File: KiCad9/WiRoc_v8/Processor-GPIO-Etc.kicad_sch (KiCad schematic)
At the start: 6 parts

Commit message: etc
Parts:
- R33, R35: LCSC Part # (none) -> C25804; Manufacturer (none) -> Uniroyal Elec; ManufacturerPartNumber (none) -> 0603WAF1002T5E
- U11: value ~ -> AllwinnerH3
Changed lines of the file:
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@@
 			)
 		)
-		(property "Value" "~"
+		(property "Value" "AllwinnerH3"
 			(at 96.52 68.58 0)
 			(effects
@@
 			)
 		)
-		(property "Value" "~"
+		(property "Value" "AllwinnerH3"
 			(at 232.41 127 0)
 			(effects
@@
 		(property "Description" ""
 			(at 254 121.92 0)
+			(effects
+				(font
+					(size 1.27 1.27)
+				)
+				(hide yes)
+			)
+		)
+		(property "LCSC Part #" "C25804"
+			(at 254 121.92 90)
+			(effects
+				(font
+					(size 1.27 1.27)
+				)
+				(hide yes)
+			)
+		)
+		(property "Manufacturer" "Uniroyal Elec"
+			(at 254 121.92 90)
+			(effects
+				(font
+					(size 1.27 1.27)
+				)
+				(hide yes)
+			)
+		)
+		(property "ManufacturerPartNumber" "0603WAF1002T5E"
+			(at 254 121.92 90)
 			(effects
 				(font
@@
 			)
 		)
+		(property "LCSC Part #" "C25804"
+			(at 251.46 114.3 90)
+			(effects
+				(font
+					(size 1.27 1.27)
+				)
+				(hide yes)
+			)
+		)
+		(property "Manufacturer" "Uniroyal Elec"
+			(at 251.46 114.3 90)
+			(effects
+				(font
+					(size 1.27 1.27)
+				)
+				(hide yes)
+			)
+		)
+		(property "ManufacturerPartNumber" "0603WAF1002T5E"
+			(at 251.46 114.3 90)
+			(effects
+				(font
+					(size 1.27 1.27)
+				)
+				(hide yes)
+			)
+		)
 		(pin "2"
 		)
@@
 			)
 		)
-		(property "Value" "~"
+		(property "Value" "AllwinnerH3"
 			(at 231.14 67.31 0)
 			(effects

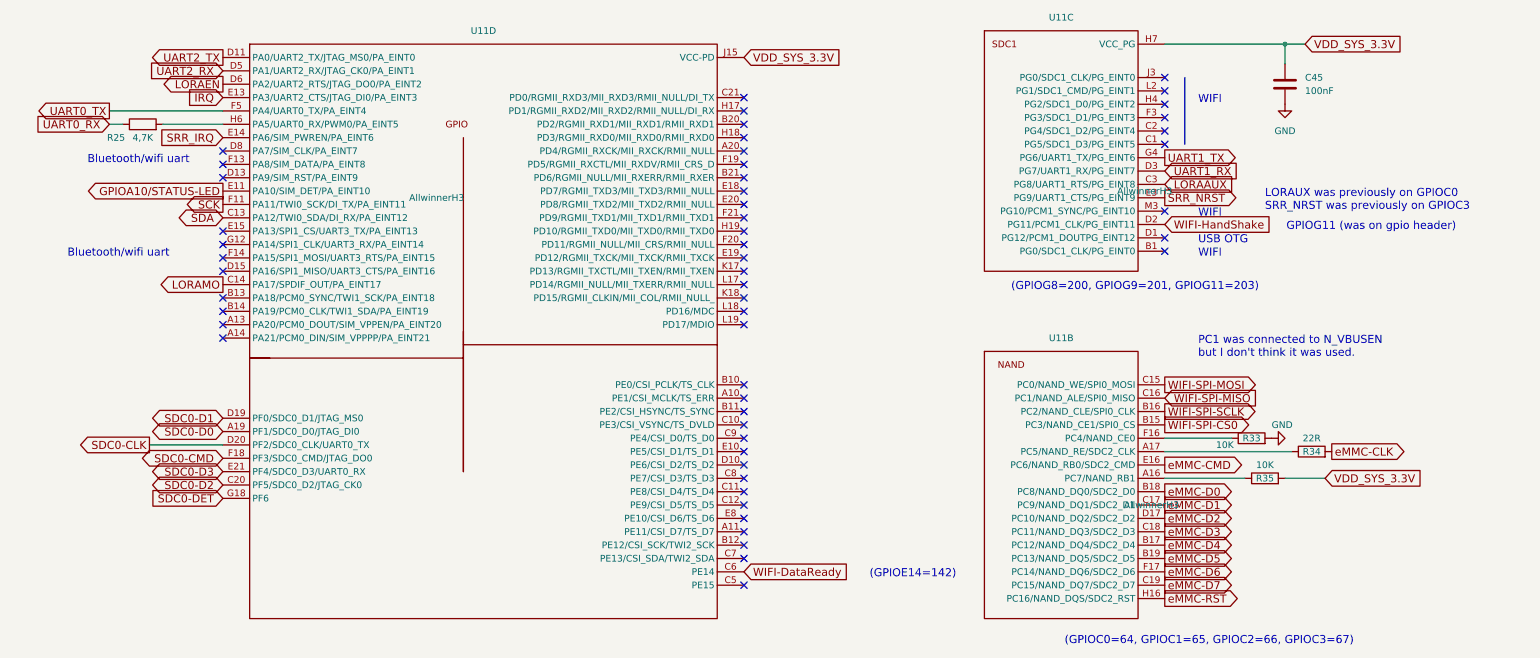
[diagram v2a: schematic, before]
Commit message: add bom
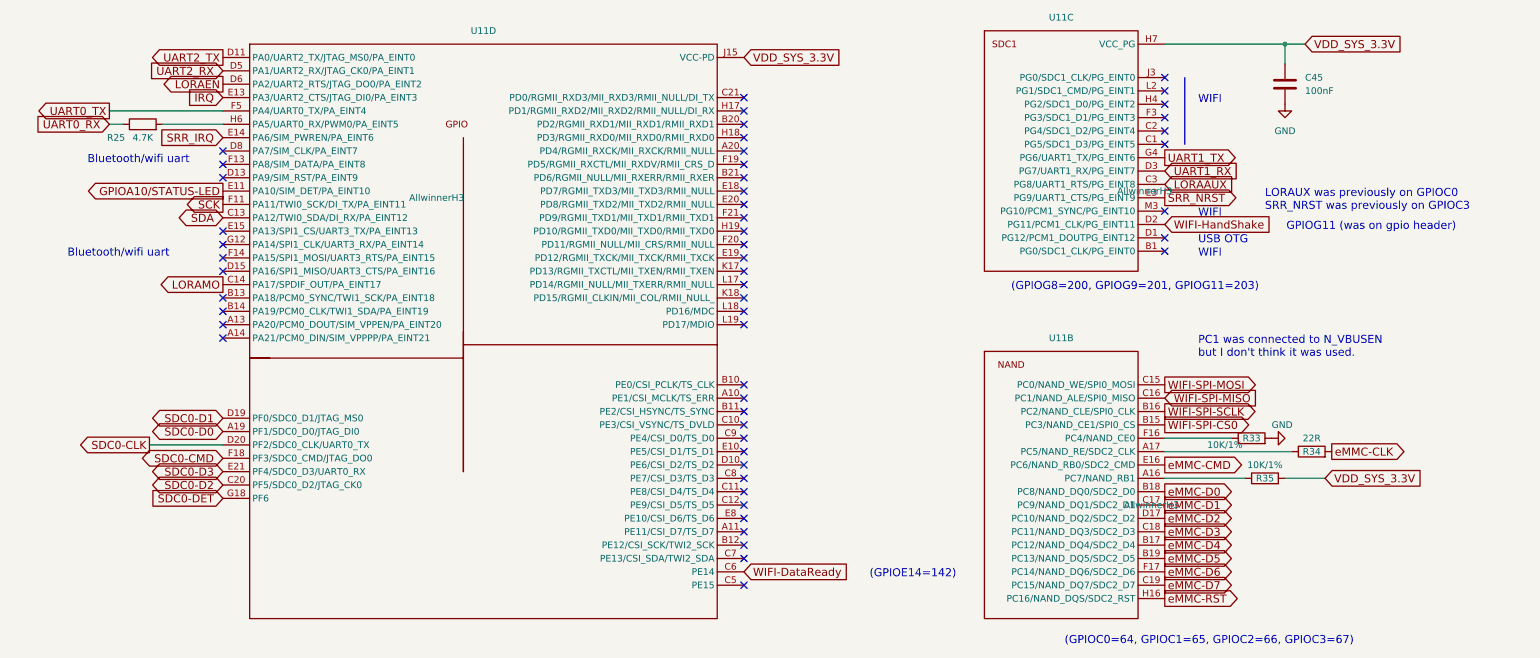
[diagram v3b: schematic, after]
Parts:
- C45: IncludeInBOM (none) -> TRUE; JLCBasicExtended (none) -> Basic; LCSC Part # (none) -> C1525; Manufacturer (none) -> Samsung Electro-Mechanics; ManufacturerPartNumber (none) -> CL05B104KO5NNNC; Package (none) -> 0402
- R25: value 4,7K -> 4.7K; IncludeInBOM (none) -> TRUE; JLCBasicExtended (none) -> Basic; LCSC Part # (none) -> C25900; Manufacturer (none) -> Uniroyal Elec; ManufacturerPartNumber (none) -> 0402WGF4701TCE; Package (none) -> 0402
- R33, R35: value 10K -> 10K/1%; IncludeInBOM (none) -> TRUE; JLCBasicExtended (none) -> Basic; LCSC Part # C25804 -> C25744; ManufacturerPartNumber 0603WAF1002T5E -> 0402WGF1002TCE; Package (none) -> 0402
- R34: IncludeInBOM (none) -> TRUE; JLCBasicExtended (none) -> Basic; LCSC Part # (none) -> C25092; Manufacturer (none) -> Uniroyal Elec; ManufacturerPartNumber (none) -> 0402WGF220JTCE; Package (none) -> 0402
- U11: IncludeInBOM (none) -> TRUE; JLCBasicExtended (none) -> Extended; LCSC Part # (none) -> C94644; Manufacturer (none) -> Allwinner; ManufacturerPartNumber (none) -> H3; Package (none) -> FBGA-347(14x14)

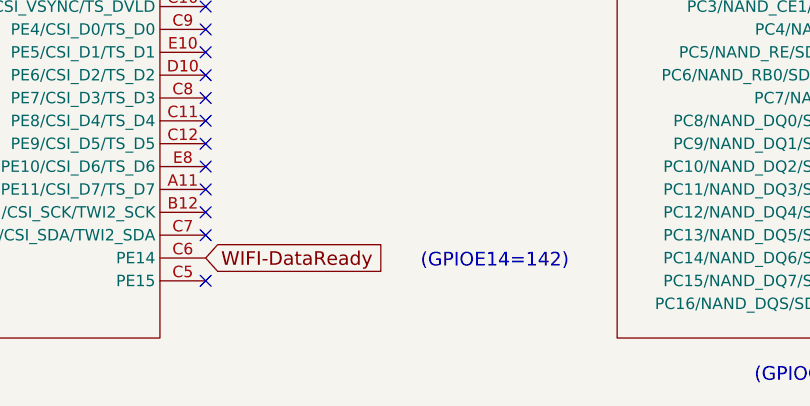
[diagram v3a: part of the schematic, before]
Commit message: add rst to wifi board
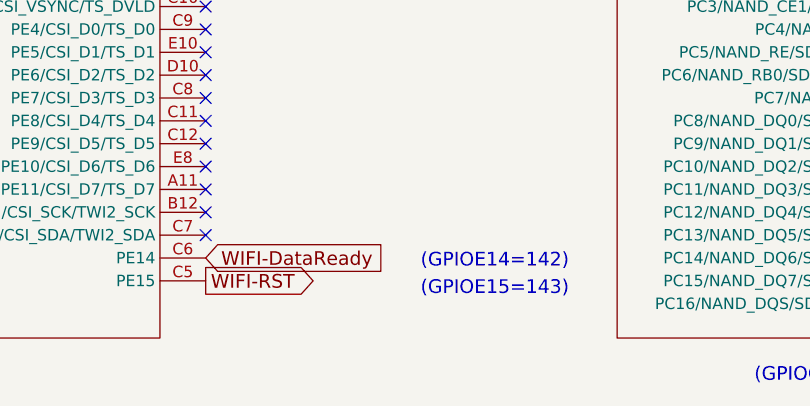
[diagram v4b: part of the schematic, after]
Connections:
- net WIFI-RST: now reaches U11.C5 (PE15)
- no-connect marks 53 -> 52
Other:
- note added: "(GPIOE15=143)"
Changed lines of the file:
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@@
+		)
+	)
+	(text "(GPIOE15=143)"
+		(exclude_from_sim no)
+		(at 178.816 144.018 0)
+		(effects
+			(font
+				(size 1.524 1.524)
+			)
+			(justify left bottom)
 		)
 	)
@@
 	)
 	(no_connect
-		(at 154.94 142.24)
-	)
-	(no_connect
 		(at 154.94 104.14)
 	)
@@
 				(hide yes)
 			)
+		)
+	)
+	(global_label "WIFI-RST"
+		(shape output)
+		(at 154.94 142.24 0)
+		(fields_autoplaced yes)
+		(effects
+			(font
+				(size 1.524 1.524)
+			)
+			(justify left)
+		)
+		(property "Intersheetrefs" "${INTERSHEET_REFS}"
+			(at 168.2596 142.24 0)
+			(effects
+				(font
+					(size 1.27 1.27)
+				)
+				(justify left)
+				(hide yes)
+			)

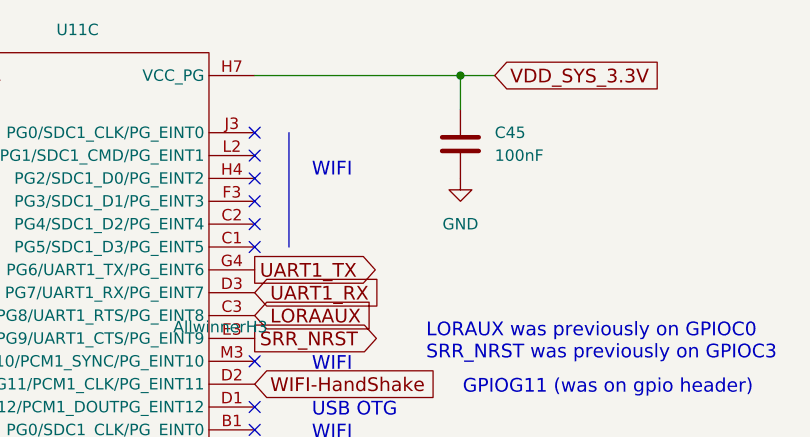
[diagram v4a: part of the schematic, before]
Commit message: change to 10uF in pdn, vdd-dram area to south caps, remove varistor, etc
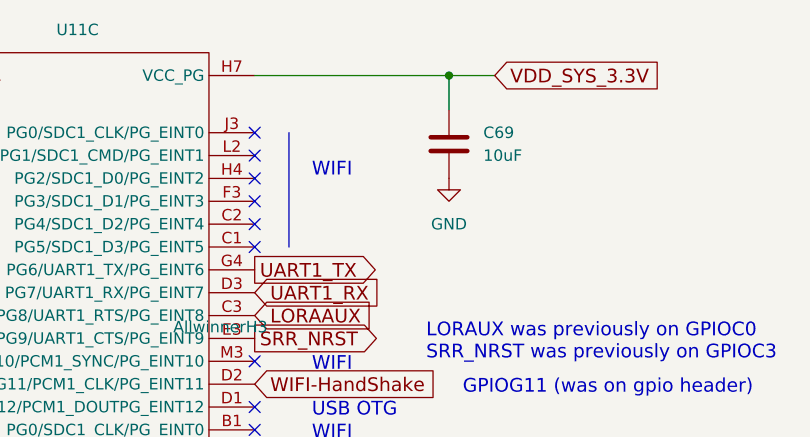
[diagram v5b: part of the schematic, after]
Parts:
- removed C45: 100nF, Capacitor_SMD:C_0402_1005Metric, symbol Device:C
- added C69: 10uF, Capacitor_SMD:C_0402_1005Metric, symbol Device:C
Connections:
- net GND: now also C69.2
- net VDD_SYS_3.3V: now also C69.1

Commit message: many small changes, change eMMC
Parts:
- C69: value 10uF -> 10uF/6.3V
- R25: value 4.7K -> 2K/1%; LCSC Part # C25900 -> C4109; ManufacturerPartNumber 0402WGF4701TCE -> 0402WGF2001TCE
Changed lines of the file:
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@@
 		(shape round)
 		(at 259.08 116.84 0)
-		(fields_autoplaced yes)
 		(effects
 			(font
@@
 		)
 		(property "Netclass" "eMMC-CLK-2"
-			(at 259.7099 114.3 0)
+			(at 259.842 114.046 0)
 			(effects
 				(font
@@
 		)
 		(property "Value" "22R"
-			(at 262.89 114.3 90)
+			(at 262.89 118.872 90)
 			(effects
 				(font
@@
 			)
 		)
-		(property "Value" "10uF"
+		(property "Value" "10uF/6.3V"
 			(at 260.35 48.26 0)
 			(effects
@@
 		(dnp no)
 		(property "Reference" "R25"
-			(at 35.56 57.15 90)
-			(effects
-				(font
-					(size 1.27 1.27)
-				)
-			)
-		)
-		(property "Value" "4.7K"
+			(at 34.036 57.15 90)
+			(effects
+				(font
+					(size 1.27 1.27)
+				)
+			)
+		)
+		(property "Value" "2K/1%"
 			(at 40.64 57.15 90)
 			(effects
@@
 			)
 		)
-		(property "LCSC Part #" "C25900"
+		(property "LCSC Part #" "C4109"
 			(at 40.64 54.61 90)
 			(effects
@@
 			)
 		)
-		(property "ManufacturerPartNumber" "0402WGF4701TCE"
+		(property "ManufacturerPartNumber" "0402WGF2001TCE"
 			(at 40.64 54.61 90)
 			(effects

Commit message: add ethernet etc
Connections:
- net WIFI-DataReady: now also U11.B13 (PA18/PCM0_SYNC/TWI1_SCK/PA_EINT18); no longer U11.C6 (PE14)
- net LORAMO: no longer names the net of U11.C14 (PA17/SPDIF_OUT/PA_EINT17)
- no-connect marks 52 -> 53
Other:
- note added: "(GPIOA18=18)"
- note added: "Was DataReady"
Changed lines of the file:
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@@
 		)
 	)
+	(text "(GPIOA18=18)"
+		(exclude_from_sim no)
+		(at 15.494 88.646 0)
+		(effects
+			(font
+				(size 1.524 1.524)
+			)
+			(justify left bottom)
+		)
+	)
+	(text "Was DataReady\n"
+		(exclude_from_sim no)
+		(at 168.402 138.938 0)
+		(effects
+			(font
+				(size 1.524 1.524)
+			)
+		)
+	)
 	(text "PC1 was connected to N_VBUSEN\nbut I don't think it was used."
 		(exclude_from_sim no)
@@
 	)
 	(no_connect
+		(at 154.94 139.7)
+	)
+	(no_connect
 		(at 154.94 54.61)
 	)
@@
 	)
 	(no_connect
-		(at 55.88 87.63)
+		(at 154.94 85.09)
 	)
 	(no_connect
-		(at 154.94 85.09)
+		(at 55.88 85.09)
 	)
 	(no_connect
@@
 		)
 	)
-	(global_label "LORAMO"
-		(shape output)
-		(at 55.88 85.09 180)
-		(fields_autoplaced yes)
-		(effects
-			(font
-				(size 1.524 1.524)
-			)
-			(justify right)
-		)
-		(property "Intersheetrefs" "${INTERSHEET_REFS}"
-			(at 44.0843 85.09 0)
-			(effects
-				(font
-					(size 1.27 1.27)
-				)
-				(justify right)
-				(hide yes)
-			)
-		)
-	)
 	(global_label "SDC0-CMD"
 		(shape bidirectional)
@@
 	(global_label "WIFI-DataReady"
 		(shape input)
-		(at 154.94 139.7 0)
+		(at 55.88 87.63 180)
 		(fields_autoplaced yes)
 		(effects
@@
 				(size 1.524 1.524)
 			)
-			(justify left)
+			(justify right)
 		)
 		(property "Intersheetrefs" "${INTERSHEET_REFS}"
-			(at 176.025 139.7 0)
+			(at 34.795 87.63 0)
 			(effects
 				(font
 					(size 1.27 1.27)
 				)
-				(justify left)
+				(justify right)
 				(hide yes)
 			)
@@
 		(on_board yes)
 		(dnp no)
-		(fields_autoplaced yes)
 		(property "Reference" "U11"
 			(at 215.265 95.25 0)
@@
 		)
 		(property "Value" "AllwinnerH3"
-			(at 232.41 127 0)
+			(at 215.646 99.822 0)
 			(effects
 				(font
@@
 	)
 	(symbol
+		(lib_name "GND_1")
 		(lib_id "power:GND")
 		(at 256.54 50.8 0)
@@
 			)
 		)
-		(property "Description" ""
+		(property "Description" "Power symbol creates a global label with name \"GND\" , ground"
 			(at 256.54 50.8 0)
 			(effects
@@
 		(on_board yes)
 		(dnp no)
-		(fields_autoplaced yes)
 		(property "Reference" "U11"
 			(at 215.265 34.29 0)
@@
 		)
 		(property "Value" "AllwinnerH3"
-			(at 231.14 67.31 0)
+			(at 213.868 39.116 0)
 			(effects
 				(font
